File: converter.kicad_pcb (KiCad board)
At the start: 2 copper layers, 106.4 x 177.8 mm, 23 parts, among them J1 A04, J2 ???, J3 A01, J4 A02, J5 A03, J6 TEENSY INTERNAL PINS, J7 Screw_Terminal_01x02, J8 BLUEFRUIT LE SPI FRIEND, K1 DIP05-1C90-51D, U1 SSTW003A0A41Z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

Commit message: removing plots
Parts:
- added R1: 100, Resistors_THT:R_Axial_DIN0204_L3.6mm_D1.6mm_P5.08mm_Vertical, F.Cu at (77.7, 202.0)
- added R2: 100, Resistors_THT:R_Axial_DIN0204_L3.6mm_D1.6mm_P5.08mm_Vertical, F.Cu at (69.6, 152.3)
- J2: value ??? -> B08
- moved J8 18.8 mm to (111.5, 189.6), turned to 0 degrees
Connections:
- K1 pad 2: /RESTORE_MAGS -> Net-(K1-Pad2)
- U1 pad 1: -48V -> +48V
- U1 pad 2: -48V -> /-VIN
- U1 pad 3: +48V -> /-VIN
- U1 pad 4: +5VD -> GNDD
- U1 pad 6: GNDD -> +5VD
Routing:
- net -48V: track 129.4 -> 103.0 mm
- net +5VD: track 524.8 -> 500.9 mm
- net /~CS: track 58.0 -> 36.3 mm
- net GNDD: track 161.7 -> 144.6 mm
- net /MISO: track 60.4 -> 44.0 mm
- net /MOSI: track 51.2 -> 35.3 mm
- net /-VIN: track 0.00 -> 14.1 mm
- net +48V: track 89.5 -> 76.6 mm
- net /IRQ: track 46.6 -> 52.3 mm
- net /SCLK: track 41.1 -> 36.3 mm
- net Net-(K1-Pad2): track 0.00 -> 3.51 mm
- net /RESET: track 51.4 -> 53.7 mm
- net /RESTORE_MAGS: track 103.4 -> 104.8 mm
- net /NUM+MULTI_I: track 105.0 -> 106.1 mm
- net Net-(D1-Pad2): track 25.5 -> 24.4 mm

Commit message: added back slik screen labels for assembly assistance
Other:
- board text added: "A"
- board text added: "B"
- board text added: "C"
- board text added: "D"
- board text added: "E"
- board text added: "F"
- board text added: "G"
- board text added: "H"
- board text added: "J"
- board text added: "K"
- board text added: "L"
- board text added: "M"
- board text added: "N"
- board text added: "P"
- board text added: "Q"
- board text added: "R"

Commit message: various varigations verified vicariously, verily verbose
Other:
- board text added: "A (X)"
- board text added: "B (X)"
- board text added: "C (X)"
- board text added: "D (X)"
- board text added: "G (X)"
- board text added: "H (X)"
- board text added: "J (X)"
- board text added: "K (X)"
- board text added: "L (X)"
- board text added: "M (X)"
- board text added: "N (X)"
- board text added: "P (X)"
- board text added: "Q (X)"
- board text added: "R (X)"

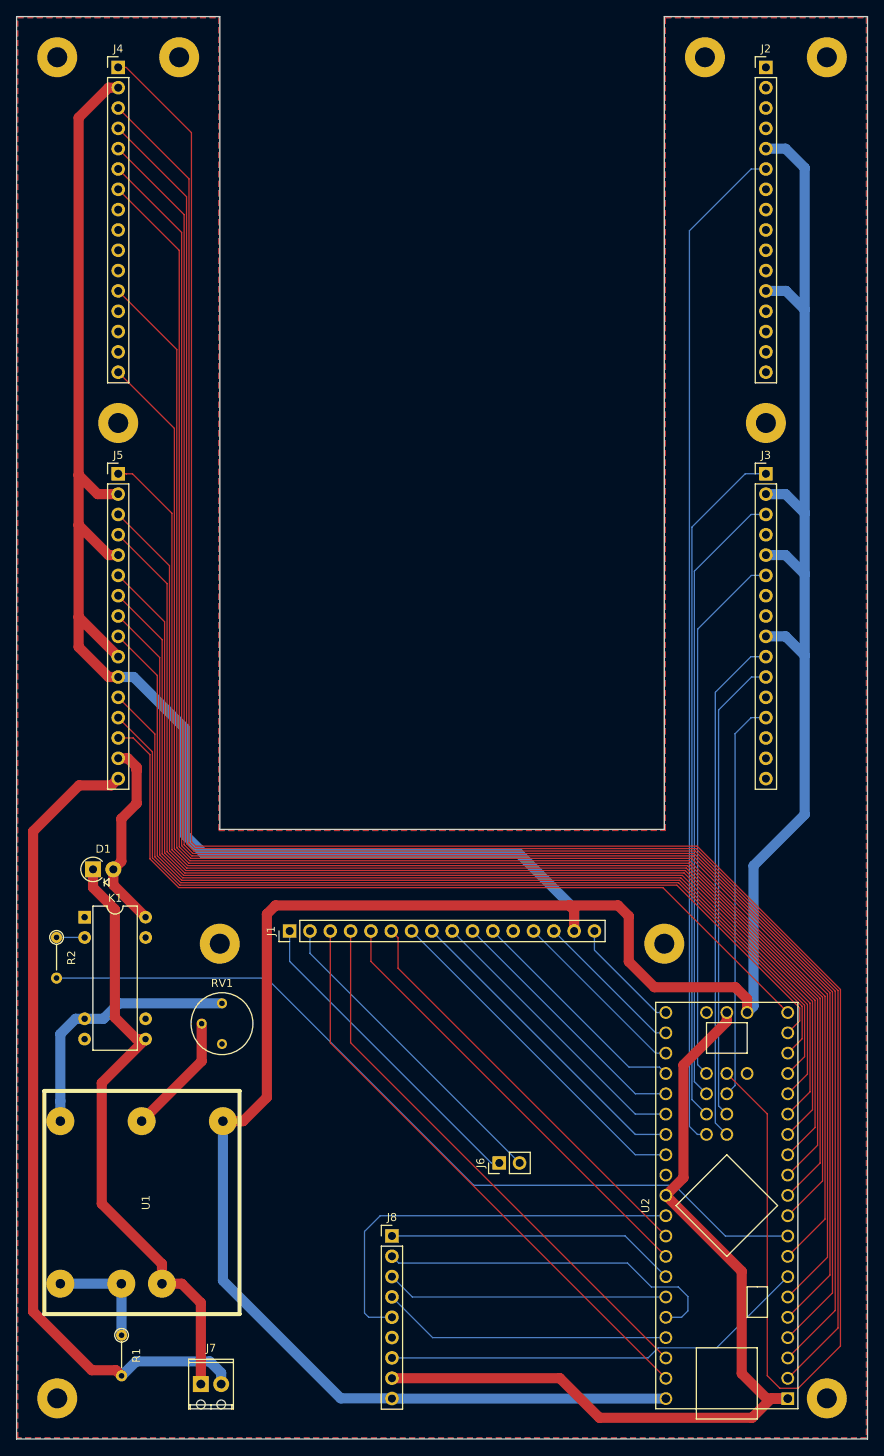
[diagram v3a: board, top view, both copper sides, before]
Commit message: updated flyback diode footprint, and cleaned up some of the silkscreening
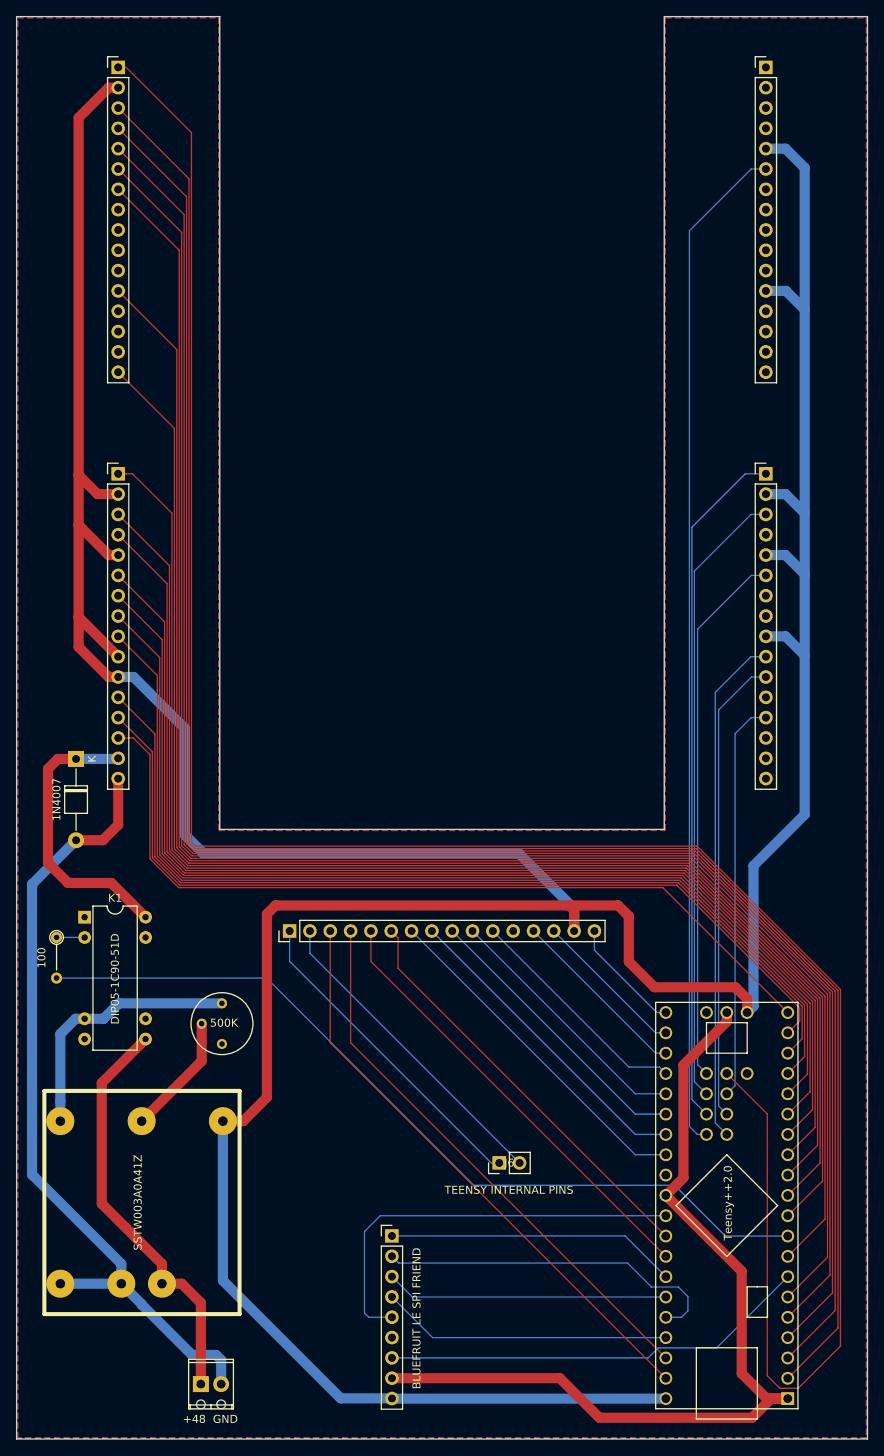
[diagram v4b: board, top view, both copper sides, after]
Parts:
- removed R1: 100, Resistors_THT:R_Axial_DIN0204_L3.6mm_D1.6mm_P5.08mm_Vertical
- removed REF** (x10): MountingHole_2.5mm_Pad, Mounting_Holes:MountingHole_2.5mm_Pad
- D1: footprint Diodes_THT:D_T-1_P2.54mm_Vertical_AnodeUp -> Diode_THT:D_T-1_P10.16mm_Horizontal
- J7: value Screw_Terminal_01x02 -> +48 GND
- moved D1 14.0 mm to (72.0, 130.0), turned to 270 degrees
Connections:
- D1 pad 1: +48V -> Net-(D1-Pad1)
- D1 pad 2: Net-(D1-Pad2) -> -48V
- J5 pad 15: Net-(D1-Pad2) -> Net-(D1-Pad1)
- K1 pad 14: Net-(D1-Pad2) -> Net-(D1-Pad1)
- U1 pad 2: /-VIN -> -48V
- U1 pad 3: /-VIN -> -48V
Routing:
- net Net-(D1-Pad1): track 0.00 -> 36.1 mm
- net +48V: track 76.6 -> 52.0 mm
- net Net-(D1-Pad2): track 24.4 -> 0.00 mm
- net /-VIN: track 14.1 -> 0.00 mm
- net -48V: track 103.0 -> 101.3 mm
